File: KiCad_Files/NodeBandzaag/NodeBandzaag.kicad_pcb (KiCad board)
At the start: 2 copper layers, 129 x 170.6 mm, 123 parts, among them J1 AC Current In, J10 Opto Coupler 1 in, J11 Opto Coupler 2 in, J12 Opto Coupler 3 in, J13 Relay 1 Output, J14 Relay 2 Output, J15 Switch 3 in, J16 Switch 2 in, J17 Switch 1 in, J18 Force output FET 1 on, J19 Force output FET 2 on, J2 Current coil in, J20 FET 1 Output, J21 FET 2 Output, J22 Force output Relay 3 on, J23 Relay 3 Output 1, J24 Relay 3 Output 2, J25 230VAC/12-40VDC in, J26 5V-in, J27 ExtDC-in, J28 Hal current sensor, J29 Current sensor select, J3 AC Current loop, J4 EXT1, J5 OledDisplay, J6 RFIDReader, J7 EXT2, J8 Force output Relay 1 on, J9 Force output Relay 2 on, K1 SANYOU_SRD_Form_C, K2 SANYOU_SRD_Form_C, K3 RT42xAxx, Q1 BC547, Q2 BC547, Q3 IRLZ34N, Q4 IRLZ34N, Q5 BC547, Q6 2N3906, U1 MCP23017_SP

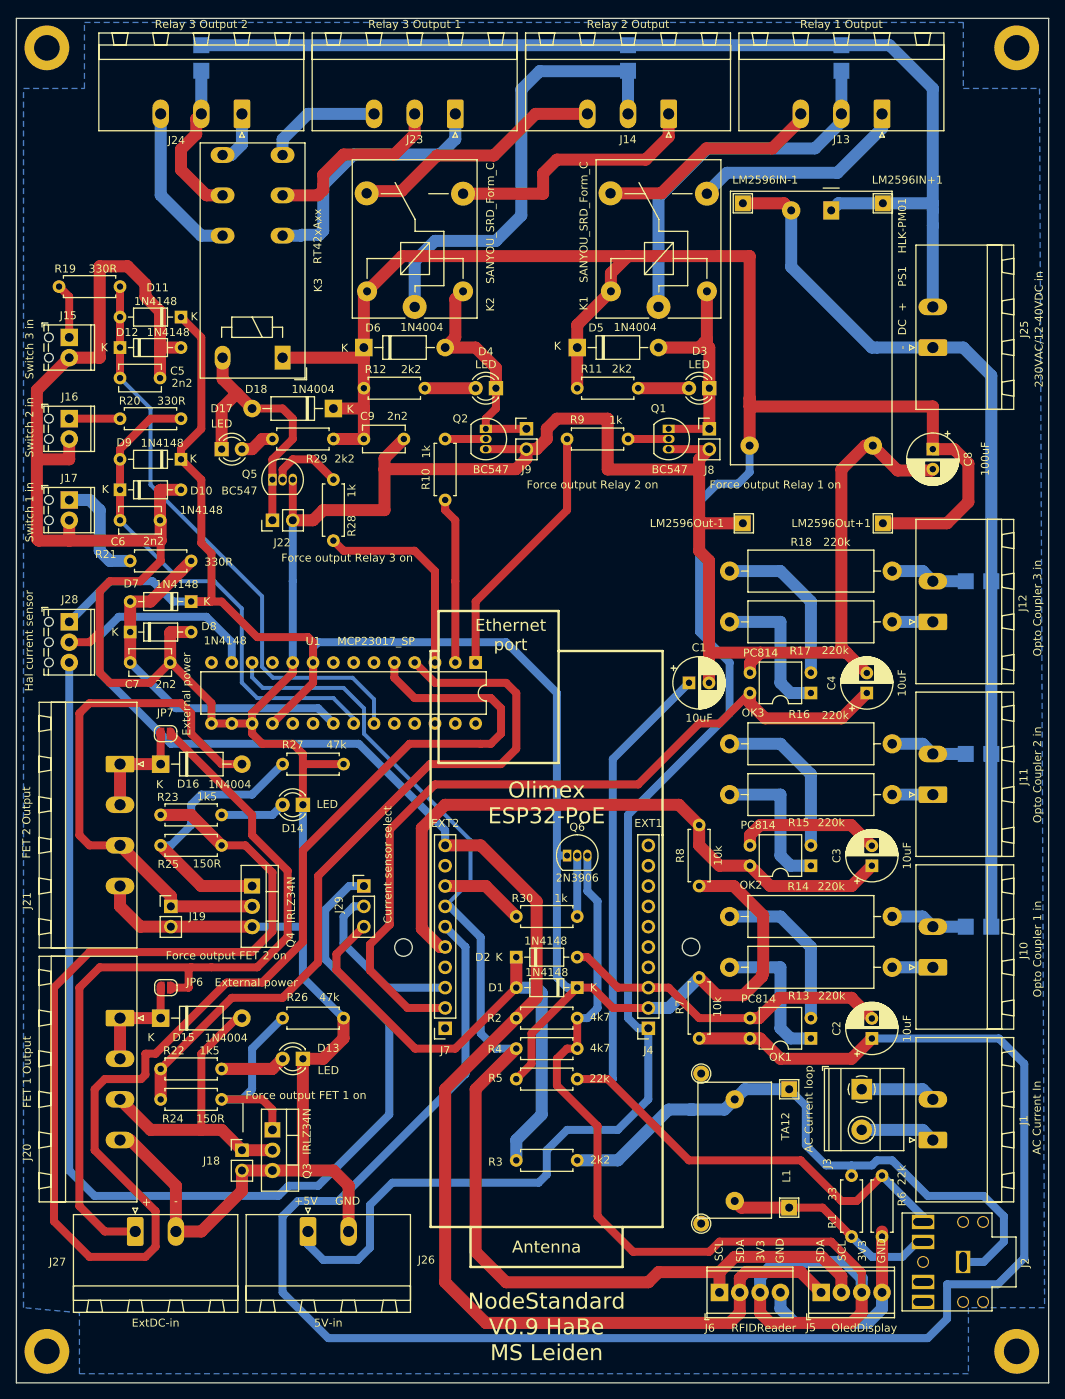
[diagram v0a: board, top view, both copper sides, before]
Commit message: V1.0.2.0 Changed the behaviour and timing e.g. when bandsaw is switched off
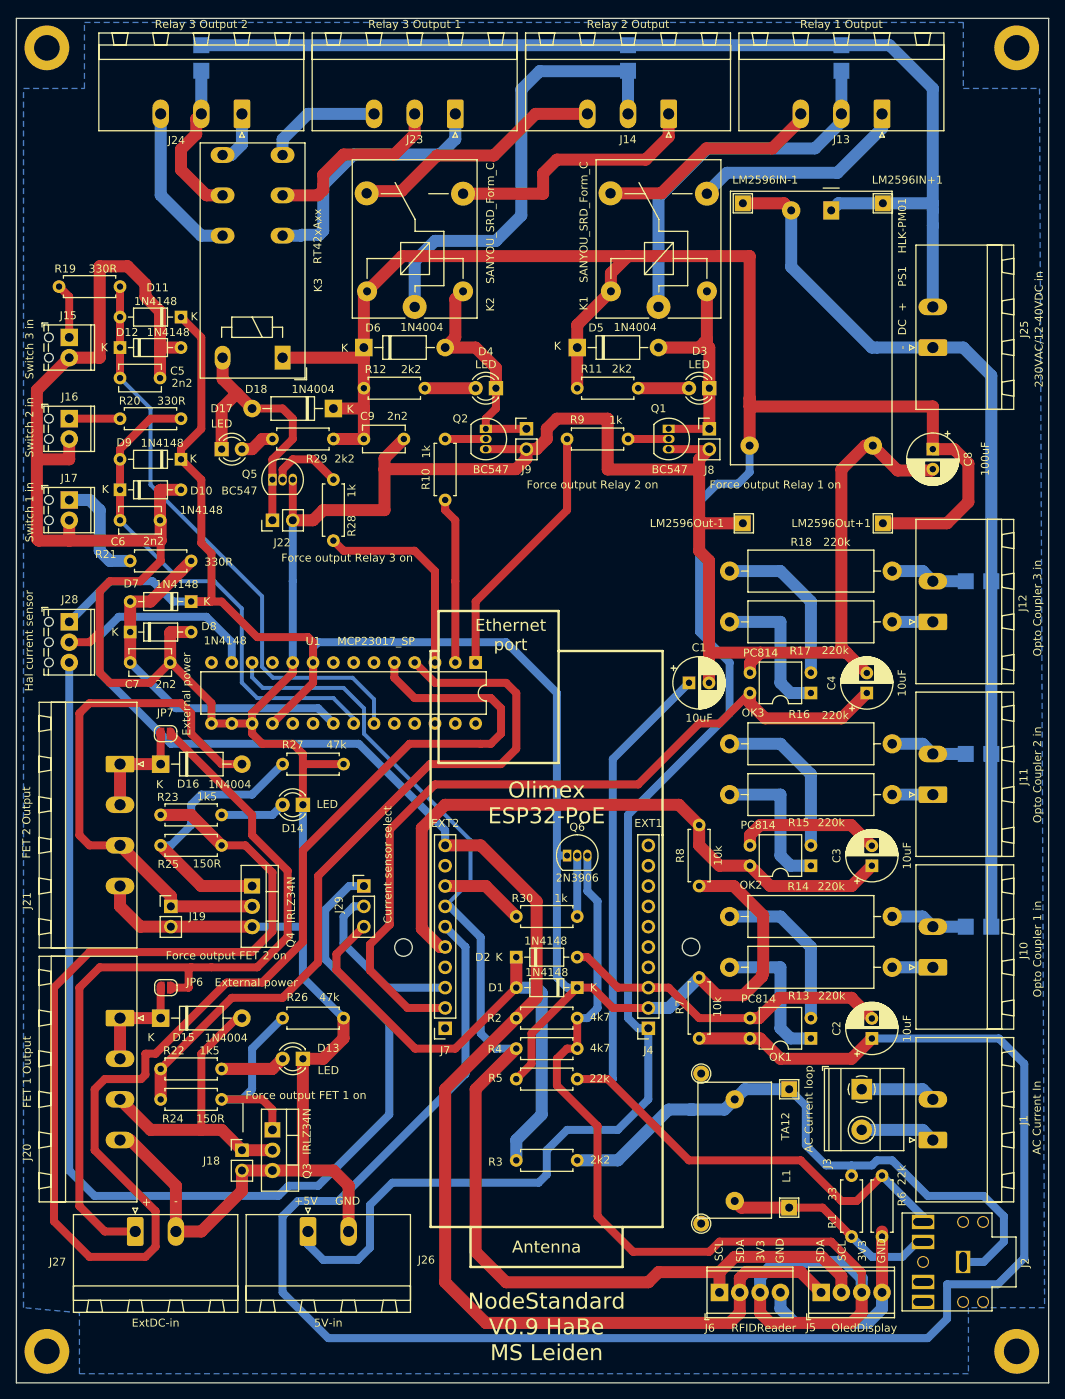
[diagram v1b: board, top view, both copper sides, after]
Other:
- net class Default removed
